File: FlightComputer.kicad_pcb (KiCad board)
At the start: 4 copper layers, 73.7 x 73.7 mm, 88 parts, among them J1 B3B-XH-A, J3 DM3D-SF, J4 12401832E402A, U1 AP62150WU-7TSOT26-WU_DIO, U2 TPS2121RUXR, U4 RP2350_60QFN, Y1 ABM8-272-T3

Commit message: fix: merge duplicate MISO0/SCLK0 nets from EAGLE restore (resolves 33 net-prefix shorts)
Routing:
- net MISO0: track 110.5 -> 0.00 mm
- net /MISO0: track 0.00 -> 110.5 mm
- net SCLK0: track 85.4 -> 0.00 mm
- net /SCLK0: track 0.00 -> 85.4 mm
- net +1V1: vias 3 -> 4
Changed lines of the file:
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@@
 	(net 2 "+3V3")
 	(net 3 "+1V1")
-	(net 4 "SCLK0")
-	(net 5 "MISO0")
 	(net 6 "/MOSI0")
 	(net 7 "unconnected-(ACCELEROMETER0-INT1-Pad5)")
@@
 		(layer "Edge.Cuts")
 	)
+	(gr_text "\n"
+		(at 153.5 93.5 0)
+		(layer "F.Cu")
+		(effects
+			(font
+				(size 1.27 1.27)
+			)
+		)
+	)
 	(segment
 		(start 163.9824 80.8696)
@@
 	)
 	(segment
+		(start 152.4951 94.5)
+		(end 152.4951 95.8511)
+		(width 0.1524)
+		(layer "F.Cu")
+		(net 3)
+	)
+	(segment
 		(start 158.1531 98.631)
 		(end 159.6871 98.631)
@@
 	(segment
 		(start 152.4951 93.8036)
-		(end 152.4951 95.8511)
+		(end 152.4951 94.5)
 		(width 0.1524)
 		(layer "F.Cu")
@@
 	)
 	(via
+		(at 152.4951 94.5)
+		(size 0.6)
+		(drill 0.3)
+		(layers "F.Cu" "B.Cu")
+		(net 3)
+	)
+	(via
 		(at 154.5971 111.3536)
 		(size 0.65)
@@
 		(width 0.2032)
 		(layer "F.Cu")
-		(net 4)
+		(net 8)
 	)
 	(segment
@@
 		(width 0.1524)
 		(layer "F.Cu")
-		(net 4)
+		(net 8)
 	)
 	(segment
@@
 		(width 0.2032)
 		(layer "F.Cu")
-		(net 4)
+		(net 8)
 	)
 	(segment
@@
 		(width 0.1524)
 		(layer "F.Cu")
-		(net 4)
+		(net 8)
 	)
 	(segment
@@
 		(width 0.1524)
 		(layer "F.Cu")
-		(net 4)
+		(net 8)
 	)
 	(segment
@@
 		(width 0.1524)
 		(layer "F.Cu")
-		(net 4)
+		(net 8)
 	)
 	(segment
@@
 		(width 0.1524)
 		(layer "F.Cu")
-		(net 4)
+		(net 8)
 	)
 	(segment
@@
 		(width 0.1524)
 		(layer "F.Cu")
-		(net 4)
+		(net 8)
 	)
 	(segment
@@
 		(width 0.1524)
 		(layer "F.Cu")
-		(net 4)
+		(net 8)
 	)
 	(segment
@@
 		(width 0.2032)
 		(layer "F.Cu")
-		(net 4)
+		(net 8)
 	)
 	(segment
@@
 		(width 0.1524)
 		(layer "F.Cu")
-		(net 4)
+		(net 8)
 	)
 	(segment
@@
 		(width 0.1524)
 		(layer "F.Cu")
-		(net 4)
+		(net 8)
 	)
 	(segment
@@
 		(width 0.1524)
 		(layer "F.Cu")
-		(net 4)
+		(net 8)
 	)
 	(segment
@@
 		(width 0.1524)
 		(layer "F.Cu")
-		(net 4)
+		(net 8)
 	)
 	(segment
@@
 		(width 0.1524)
 		(layer "F.Cu")
-		(net 4)
+		(net 8)
 	)
 	(segment
@@
 		(width 0.1524)
 		(layer "F.Cu")
-		(net 4)
+		(net 8)
 	)
 	(segment
@@
 		(width 0.1524)
 		(layer "F.Cu")
-		(net 4)
+		(net 8)
 	)
 	(segment
@@
 		(width 0.1524)
 		(layer "B.Cu")
-		(net 4)
+		(net 8)
 	)
 	(segment
@@
 		(width 0.1524)
 		(layer "B.Cu")
-		(net 4)
+		(net 8)
 	)
 	(segment
@@
 		(width 0.1524)
 		(layer "B.Cu")
-		(net 4)
+		(net 8)
 	)
 	(segment
@@
 		(width 0.1524)
 		(layer "B.Cu")
-		(net 4)
+		(net 8)
 	)
 	(segment
@@
 		(width 0.1524)
 		(layer "B.Cu")
-		(net 4)
+		(net 8)
 	)
 	(segment
@@
 		(width 0.1524)
 		(layer "B.Cu")
-		(net 4)
+		(net 8)
 	)
 	(segment
@@
 		(width 0.1524)
 		(layer "B.Cu")
-		(net 4)
+		(net 8)
 	)
 	(segment
@@
 		(width 0.1524)
 		(layer "B.Cu")
-		(net 4)
+		(net 8)
 	)
 	(segment
@@
 		(width 0.1524)
 		(layer "B.Cu")
-		(net 4)
+		(net 8)
 	)
 	(segment
@@
 		(width 0.1524)
 		(layer "B.Cu")
-		(net 4)
+		(net 8)
 	)
 	(segment
@@
 		(width 0.1524)
 		(layer "F.Cu")
-		(net 5)
+		(net 11)
 	)
 	(segment
@@
 		(width 0.1524)
 		(layer "F.Cu")
-		(net 5)
+		(net 11)
 	)
 	(segment
@@
 		(width 0.1524)
 		(layer "F.Cu")
-		(net 5)
+		(net 11)
 	)
 	(segment
@@
 		(width 0.1524)
 		(layer "F.Cu")
-		(net 5)
+		(net 11)
 	)
 	(segment
@@
 		(width 0.1524)
 		(layer "F.Cu")
-		(net 5)
+		(net 11)
 	)
 	(segment
@@
 		(width 0.1524)
 		(layer "F.Cu")
-		(net 5)
+		(net 11)
 	)
 	(segment
@@
 		(width 0.1524)
 		(layer "F.Cu")
-		(net 5)
+		(net 11)
 	)
 	(segment
@@
 		(width 0.1524)
 		(layer "F.Cu")
-		(net 5)
+		(net 11)
 	)
 	(segment
@@
 		(width 0.1524)
 		(layer "F.Cu")
-		(net 5)
+		(net 11)
 	)
 	(segment
@@
 		(width 0.1524)
 		(layer "F.Cu")
-		(net 5)
+		(net 11)
 	)
 	(segment
@@
 		(width 0.1524)
 		(layer "F.Cu")
-		(net 5)
+		(net 11)
 	)
 	(segment
@@
 		(width 0.1524)
 		(layer "F.Cu")
-		(net 5)
+		(net 11)
 	)
 	(segment
@@
 		(width 0.1524)
 		(layer "F.Cu")
-		(net 5)
+		(net 11)
 	)
 	(segment
@@
 		(width 0.1524)
 		(layer "F.Cu")
-		(net 5)
+		(net 11)
 	)
 	(segment
@@
 		(width 0.1524)
 		(layer "F.Cu")
-		(net 5)
+		(net 11)
 	)
 	(segment
@@
 		(width 0.1524)
 		(layer "F.Cu")
-		(net 5)
+		(net 11)
 	)
 	(segment
@@
 		(width 0.1524)
 		(layer "F.Cu")
-		(net 5)
+		(net 11)
 	)
 	(segment
@@
 		(width 0.1524)
 		(layer "F.Cu")
-		(net 5)
+		(net 11)
 	)
 	(segment
@@
 		(width 0.1524)
 		(layer "F.Cu")
-		(net 5)
+		(net 11)
 	)
 	(segment
@@
 		(width 0.1524)
 		(layer "F.Cu")
-		(net 5)
+		(net 11)
 	)
 	(segment
@@
 		(width 0.1524)
 		(layer "F.Cu")
-		(net 5)
+		(net 11)
 	)
 	(segment
@@
 		(width 0.1524)
 		(layer "F.Cu")
-		(net 5)
+		(net 11)
 	)
 	(segment
@@
 		(width 0.1524)
 		(layer "F.Cu")
-		(net 5)
+		(net 11)
 	)
 	(segment
@@
 		(width 0.1524)
 		(layer "F.Cu")
-		(net 5)
+		(net 11)
 	)
 	(segment
@@
 		(width 0.1524)
 		(layer "F.Cu")
-		(net 5)
+		(net 11)
 	)
 	(segment
@@
 		(width 0.1524)
 		(layer "F.Cu")
-		(net 5)
+		(net 11)
 	)
 	(segment
@@
 		(width 0.1524)
 		(layer "F.Cu")
-		(net 5)
+		(net 11)
 	)
 	(segment
@@
 		(width 0.1524)
 		(layer "B.Cu")
-		(net 5)
+		(net 11)
 	)
 	(segment
@@
 		(width 0.2)
 		(layer "B.Cu")
-		(net 5)
+		(net 11)
 	)
 	(segment
@@
 		(width 0.1524)
 		(layer "B.Cu")
-		(net 5)
+		(net 11)
 	)
 	(segment
@@
 		(width 0.1524)
 		(layer "B.Cu")
-		(net 5)
+		(net 11)
 	)
 	(segment
@@
 		(width 0.1524)
 		(layer "B.Cu")
-		(net 5)
+		(net 11)
 	)
 	(segment
@@
 		(width 0.2)
 		(layer "B.Cu")
-		(net 5)
+		(net 11)
 	)
 	(segment
@@
 		(width 0.1524)
 		(layer "B.Cu")
-		(net 5)
+		(net 11)
 	)
 	(segment

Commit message: fixed a wrongly imported via
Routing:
- net GND: track 118.5 -> 116.0 mm, vias 12 -> 11

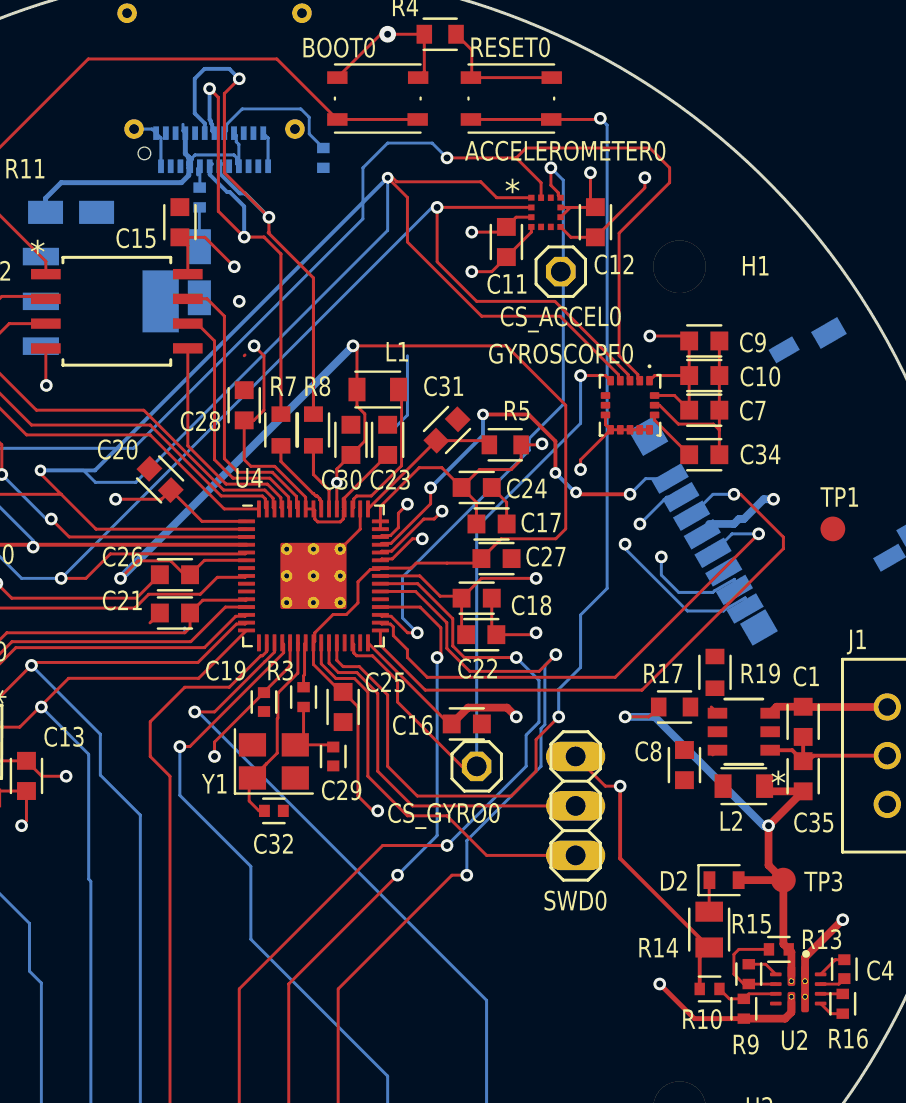
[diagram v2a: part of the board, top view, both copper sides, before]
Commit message: Trace Fixing
Changed some traces to flow more smoothly. Board is still incomplete. 8/13.
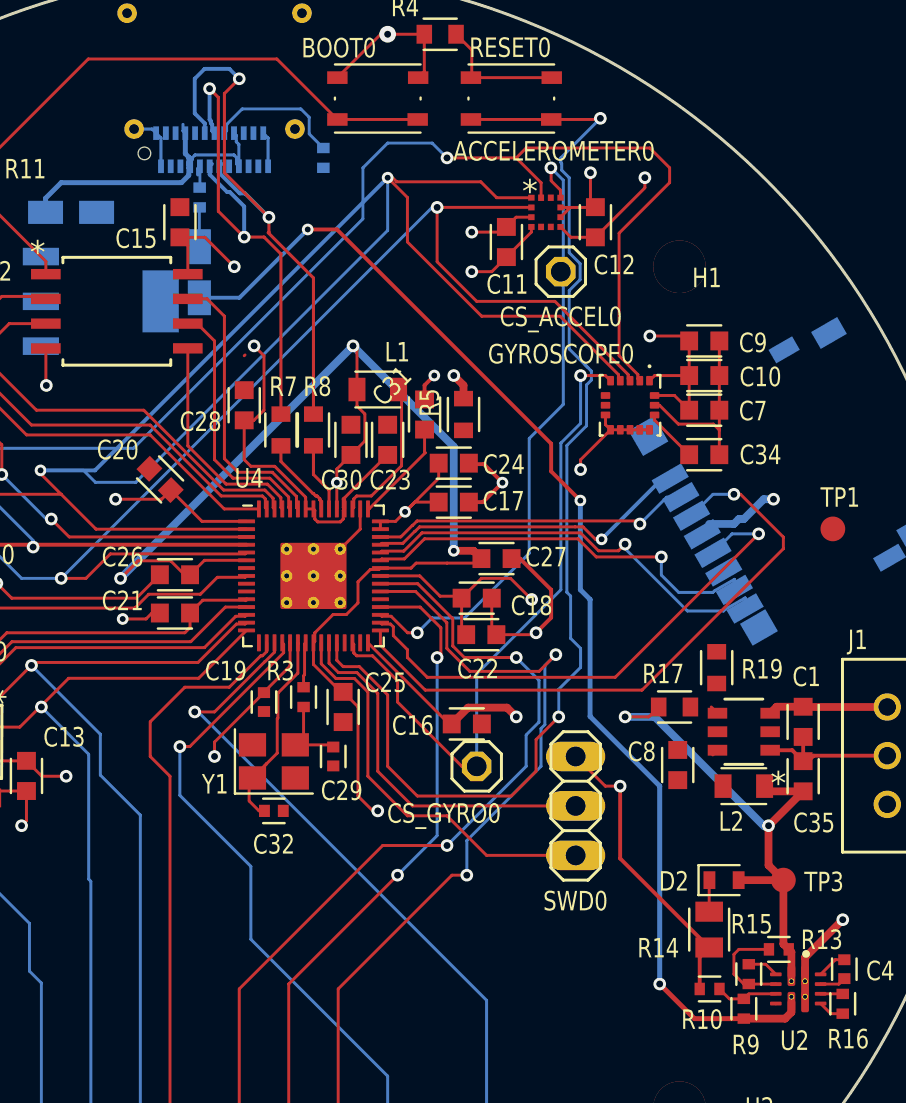
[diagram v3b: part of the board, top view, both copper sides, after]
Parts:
- moved R5 2.65 mm to (159.0, 91.0), turned to 90 degrees
- moved C17 2.24 mm to (158.5, 95.5)
- moved C24 1.72 mm to (158.5, 93.5)
- moved C31 1.40 mm to (157.0, 91.0), turned to -90 degrees
- moved C8 0.35 mm to (170.0, 109.0)
- moved R19 0.26 mm to (172.0, 104.0)
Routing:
- net /+3V3_USB: track 8.16 -> 62.3 mm, vias 2 -> 3
- net /SDIO_D0: track 8.40 -> 21.1 mm, vias 2 -> 1
- net /SDIO_D3: track 5.19 -> 16.6 mm, vias 2 -> 1
- net /SDIO_D1: track 12.5 -> 22.0 mm, vias 2 -> 1
- net +1V1: track 78.6 -> 69.3 mm, vias 4 -> 5
- net +3V3: track 147.0 -> 141.0 mm, vias 18 -> 19
- net GND: track 116.0 -> 121.6 mm, vias 11 -> 14
- net /SDIO_D2: track 21.7 -> 16.8 mm, vias 5 -> 1
- net /VREG_AVDD: track 7.77 -> 5.34 mm
- net /RUN: track 58.5 -> 60.8 mm

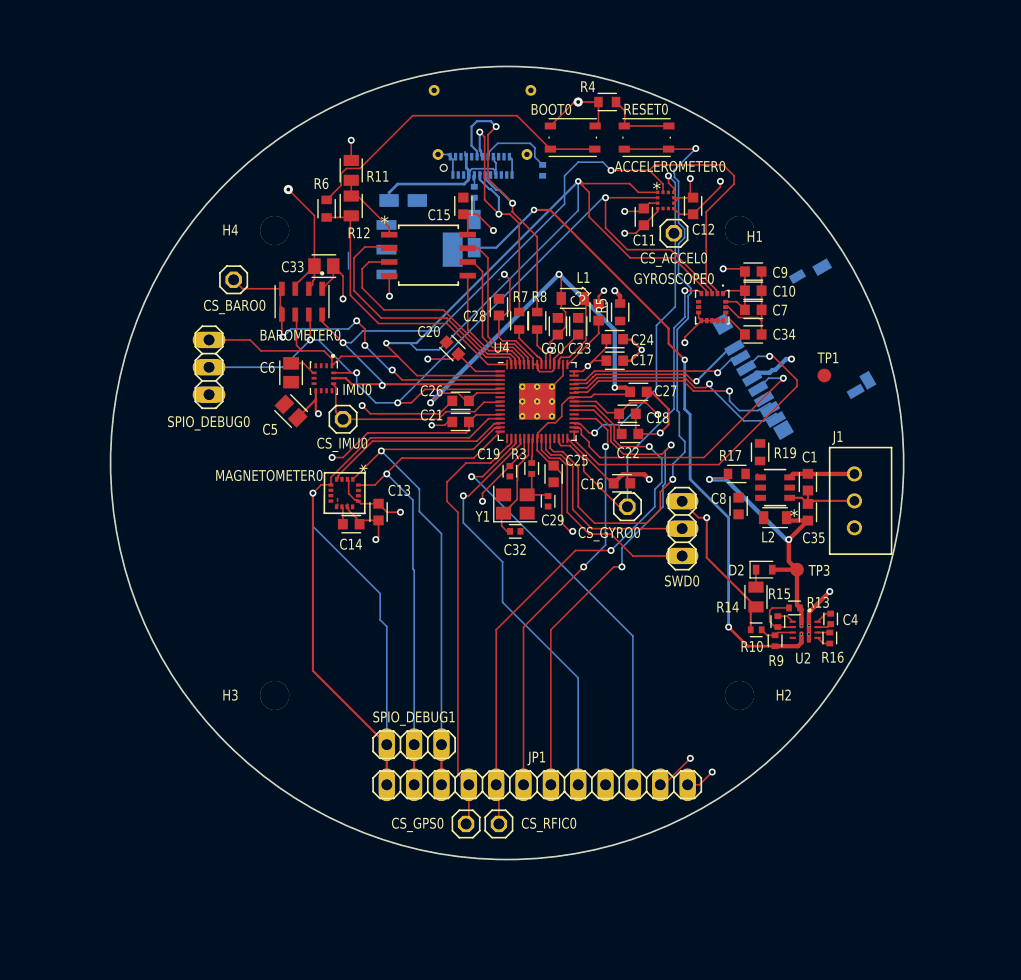
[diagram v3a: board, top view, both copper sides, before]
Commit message: Logos Added
Eclipse logo added on front, Rice shield added on back. Changes are cosmetic only.
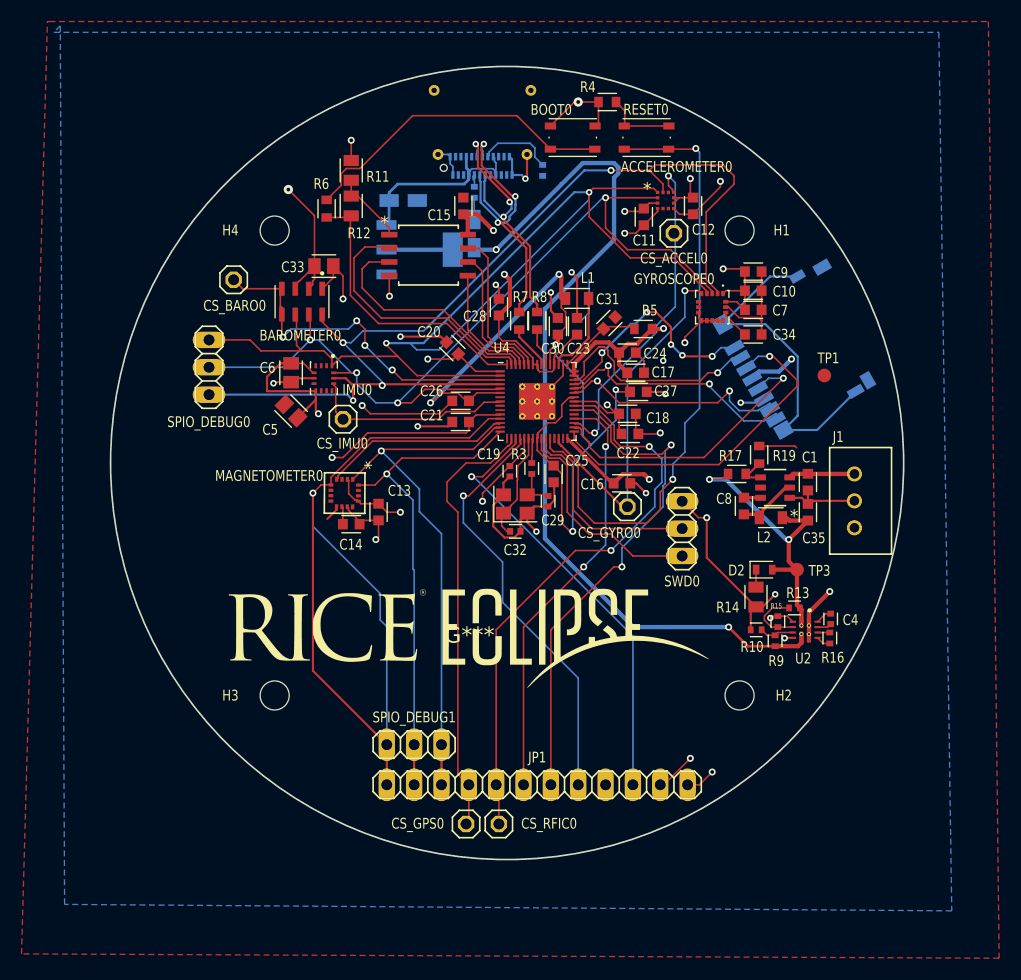
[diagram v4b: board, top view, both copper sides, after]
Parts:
- added G***: LOGO, LOGO, F.Cu at (145.0, 121.0)
- added G***: LOGO, LOGO, B.Cu at (135.5, 115.0)
- moved R5 2.65 mm to (161.1, 92.6), turned to 0 degrees
- moved C17 2.24 mm to (160.4, 96.6)
- moved C24 1.72 mm to (159.7, 94.7)
- moved C31 1.41 mm to (158.0, 92.0), turned to -135 degrees
- moved C8 0.50 mm to (170.5, 109.0)
- moved L1 0.40 mm to (155.0, 89.7)
- moved L2 0.39 mm to (173.0, 110.1)
- moved R19 0.26 mm to (171.9, 104.2)
- moved C23 0.11 mm to (155.0, 92.3)
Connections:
- R17 pad 2: Net-(R17-Pad2) -> Net-(U1-FB)
- R19 pad 1: Net-(R17-Pad2) -> Net-(U1-FB)
- U1 pad 4: unconnected-(U1-FB-Pad4) -> Net-(U1-FB)
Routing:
- net GND: track 121.6 -> 169.0 mm, vias 14 -> 26
- net Net-(J3-SHIELD-PadS1): track 0.00 -> 32.6 mm
- net /+3V3_USB: track 62.3 -> 91.4 mm, vias 3 -> 2
- net /SCLK0: track 85.4 -> 98.4 mm, vias 3 -> 4
- net +3V3: track 141.0 -> 153.5 mm, vias 19 -> 18
- net +1V1: track 69.3 -> 76.9 mm
- net Net-(U1-SW): track 0.07 -> 5.27 mm
- net /USB_N: track 29.2 -> 24.7 mm, vias 2 -> 3
- net /SDIO_D3: track 16.6 -> 20.9 mm
- net /SDIO_D2: track 16.8 -> 21.1 mm, vias 1 -> 5
- net Net-(U1-FB): track 0.00 -> 3.18 mm
- net /MISO0: track 110.5 -> 108.0 mm
- net /VREG_AVDD: track 5.34 -> 7.77 mm
- net /RUN: track 60.8 -> 58.5 mm
- net /V_USB: track 16.4 -> 18.3 mm
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- added copper zone on B.Cu, net GND
- added copper zone on F.Cu, net GND

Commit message: Reduced board size to 2.5in
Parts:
- removed C1: 10uF, FlightComputer:CAPC1608X85
- removed C35: 22uF, FlightComputer:CAPC1608X85
- removed C8: 100nF, FlightComputer:CAPC1608X85
- removed H1, H2, H3: MountingHole, FlightComputer:MOUNTINGHOLE_MOUNTINGHOLE_2.7MM_M2.5
- removed J1: B3B-XH-A, FlightComputer:B3B-XH-A
- removed L2: 3.3uH, FlightComputer:INDC2009X120
- removed R17: 31.6k, FlightComputer:RESC1608X60
- removed R19: 10k, FlightComputer:RESC1608X60
- removed U1: AP62150WU-7TSOT26-WU_DIO, FlightComputer:TSOT26-WU_DIO
- added H10: MountingHole, FlightComputer:MOUNTINGHOLE_MOUNTINGHOLE_2.7MM_M2.5, F.Cu at (-102.5, -55.8)
- added H11: MountingHole, FlightComputer:MOUNTINGHOLE_MOUNTINGHOLE_2.7MM_M2.5, F.Cu at (-31.6, 147.2)
- added H12: MountingHole, FlightComputer:MOUNTINGHOLE_MOUNTINGHOLE_2.7MM_M2.5, F.Cu at (131.4, 116.2)
- added H13: MountingHole, FlightComputer:MOUNTINGHOLE_MOUNTINGHOLE_2.7MM_M2.5, F.Cu at (60.5, -86.8)
- added H14: MountingHole, FlightComputer:MOUNTINGHOLE_MOUNTINGHOLE_2.7MM_M2.5, F.Cu at (-142.6, -15.8)
- added H15: MountingHole, FlightComputer:MOUNTINGHOLE_MOUNTINGHOLE_2.7MM_M2.5, F.Cu at (-71.5, 187.2)
- added H16: MountingHole, FlightComputer:MOUNTINGHOLE_MOUNTINGHOLE_2.7MM_M2.5, F.Cu at (171.4, 118.2)
- added H17: MountingHole, FlightComputer:MOUNTINGHOLE_MOUNTINGHOLE_2.7MM_M2.5, F.Cu at (100.5, -86.8)
- added H18: MountingHole, FlightComputer:MOUNTINGHOLE_MOUNTINGHOLE_2.7MM_M2.5, F.Cu at (-102.5, -15.8)
- added H4: MountingHole, FlightComputer:MOUNTINGHOLE_MOUNTINGHOLE_2.7MM_M2.5, F.Cu at (133.4, 76.2)
- added H5: MountingHole, FlightComputer:MOUNTINGHOLE_MOUNTINGHOLE_2.7MM_M2.5, F.Cu at (60.5, -126.8)
- added H6: MountingHole, FlightComputer:MOUNTINGHOLE_MOUNTINGHOLE_2.7MM_M2.5, F.Cu at (-142.6, -55.8)
- added H7: MountingHole, FlightComputer:MOUNTINGHOLE_MOUNTINGHOLE_2.7MM_M2.5, F.Cu at (-71.5, 147.2)
- added H8: MountingHole, FlightComputer:MOUNTINGHOLE_MOUNTINGHOLE_2.7MM_M2.5, F.Cu at (171.4, 76.2)
- added H9: MountingHole, FlightComputer:MOUNTINGHOLE_MOUNTINGHOLE_2.7MM_M2.5, F.Cu at (100.5, -126.8)
- moved H19 189.4 mm to (-31.6, 187.2)
- moved G*** 29.7 mm to (121.0, 138.5)
- moved G*** 24.0 mm to (111.5, 115.0)
- moved SPIO_DEBUG1 11.5 mm to (140.0, 119.6)
- moved CS_GPS0 11.5 mm to (144.8, 127.0)
- moved CS_RFIC0 11.5 mm to (147.8, 127.0)
- moved JP1 11.5 mm to (151.4, 123.4)
- moved C4 8.19 mm to (174.7, 112.3)
- moved D2 8.19 mm to (168.5, 107.7)
- moved R10 8.19 mm to (167.7, 113.3)
- moved R14 8.19 mm to (167.7, 110.2)
- moved R15 8.19 mm to (169.7, 112.5)
- moved R9 8.19 mm to (169.5, 114.3)
- moved R13 8.19 mm to (171.3, 111.3)
- moved R16 8.19 mm to (174.6, 114.1)
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- renumbered H4 to H19
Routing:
- net /MISO1: track 80.5 -> 40.5 mm
- net /+3V3_USB: track 91.4 -> 73.7 mm
- net /+3V3_VBAT: track 26.5 -> 9.10 mm, vias 2 -> 1
- net GND: track 169.0 -> 151.6 mm, vias 26 -> 27
- net /RF_GPIO2: track 48.5 -> 36.5 mm
- net /SCLK0: track 98.4 -> 86.4 mm
- net /RF_GPIO0: track 39.7 -> 28.2 mm
- net /CS_RFIC: track 53.3 -> 41.8 mm
- net /MOSI1: track 48.9 -> 37.4 mm
- net /CS_GPS: track 40.6 -> 29.1 mm
- net /SCLK1: track 52.7 -> 41.3 mm
- net /LNA_EN_LP: track 40.8 -> 29.3 mm
- net /RF_GPIO3: track 39.1 -> 28.9 mm
- net /SDIO_CMD: track 32.1 -> 22.7 mm
- net /+7.4V: track 6.16 -> 0.00 mm
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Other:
- board size 73.7 x 73.7 mm -> 61 x 61 mm
